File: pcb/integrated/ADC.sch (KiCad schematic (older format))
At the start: 18 parts, among them U6001 SG3225, U6002 AD9609

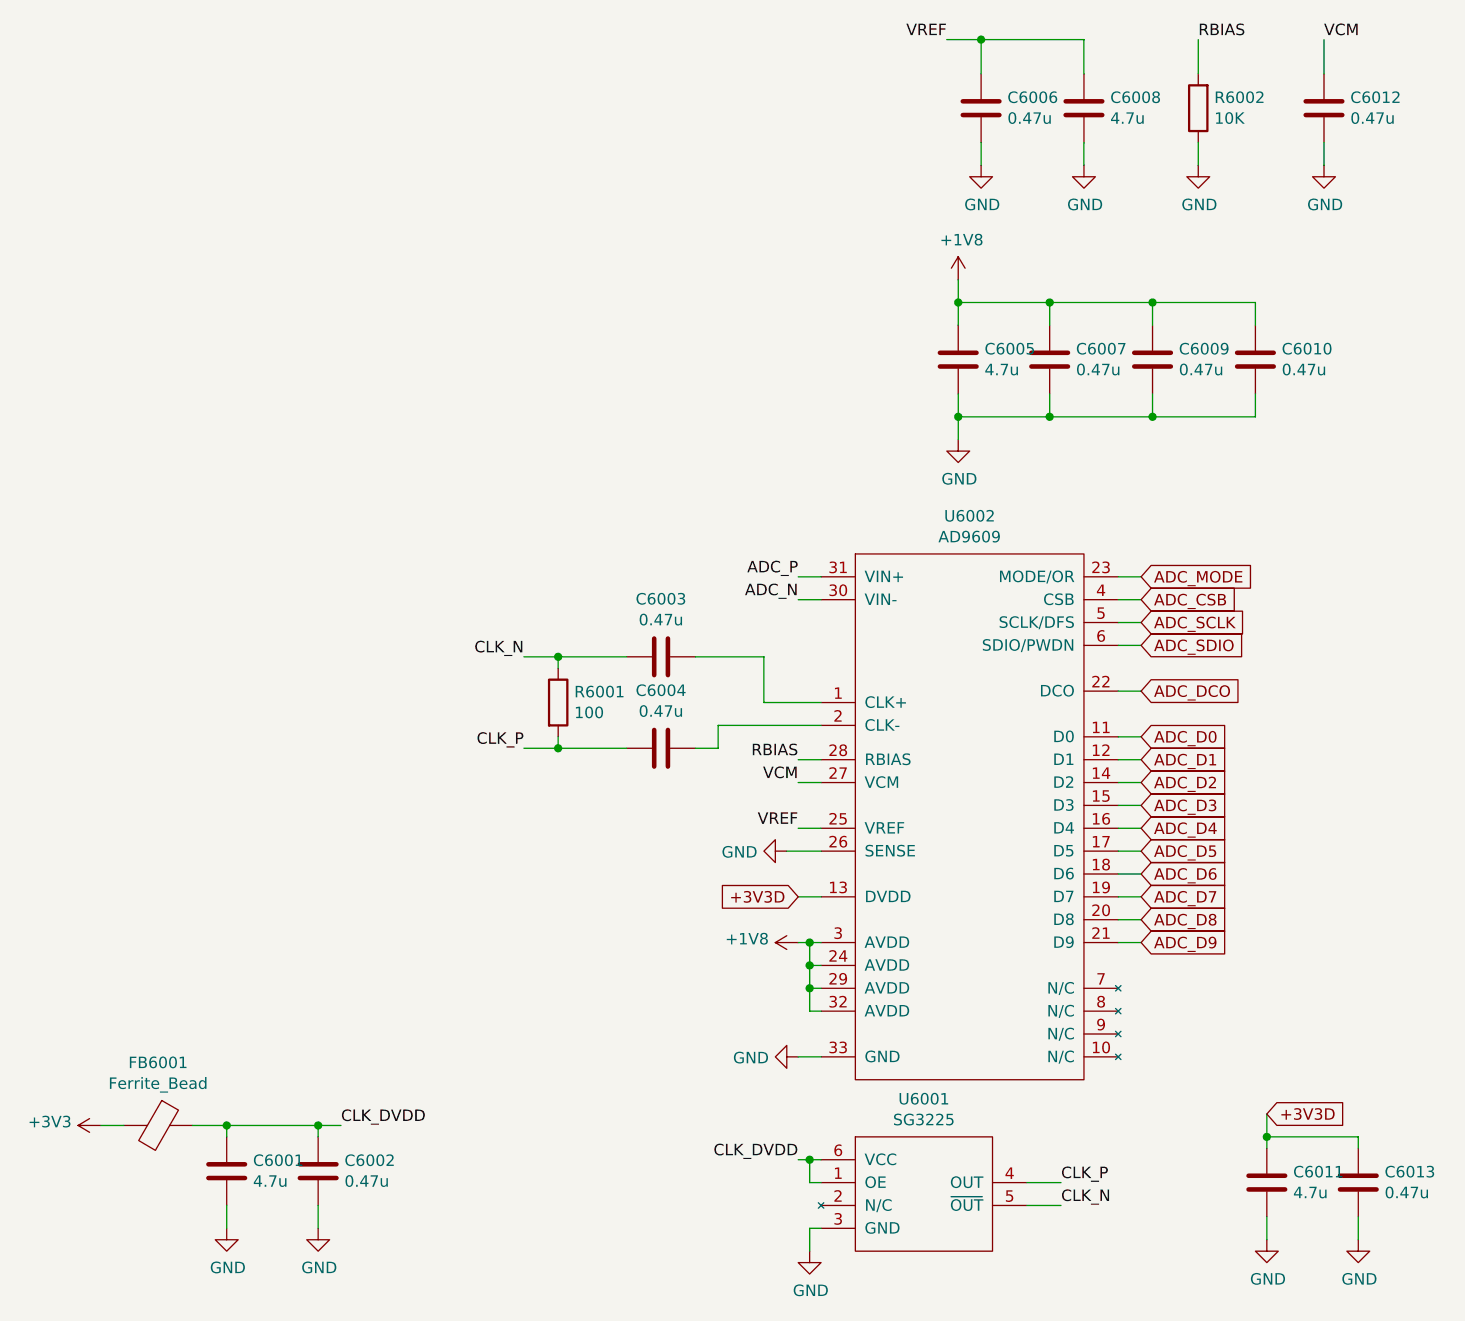
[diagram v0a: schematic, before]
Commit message: schematic fixes and component placement
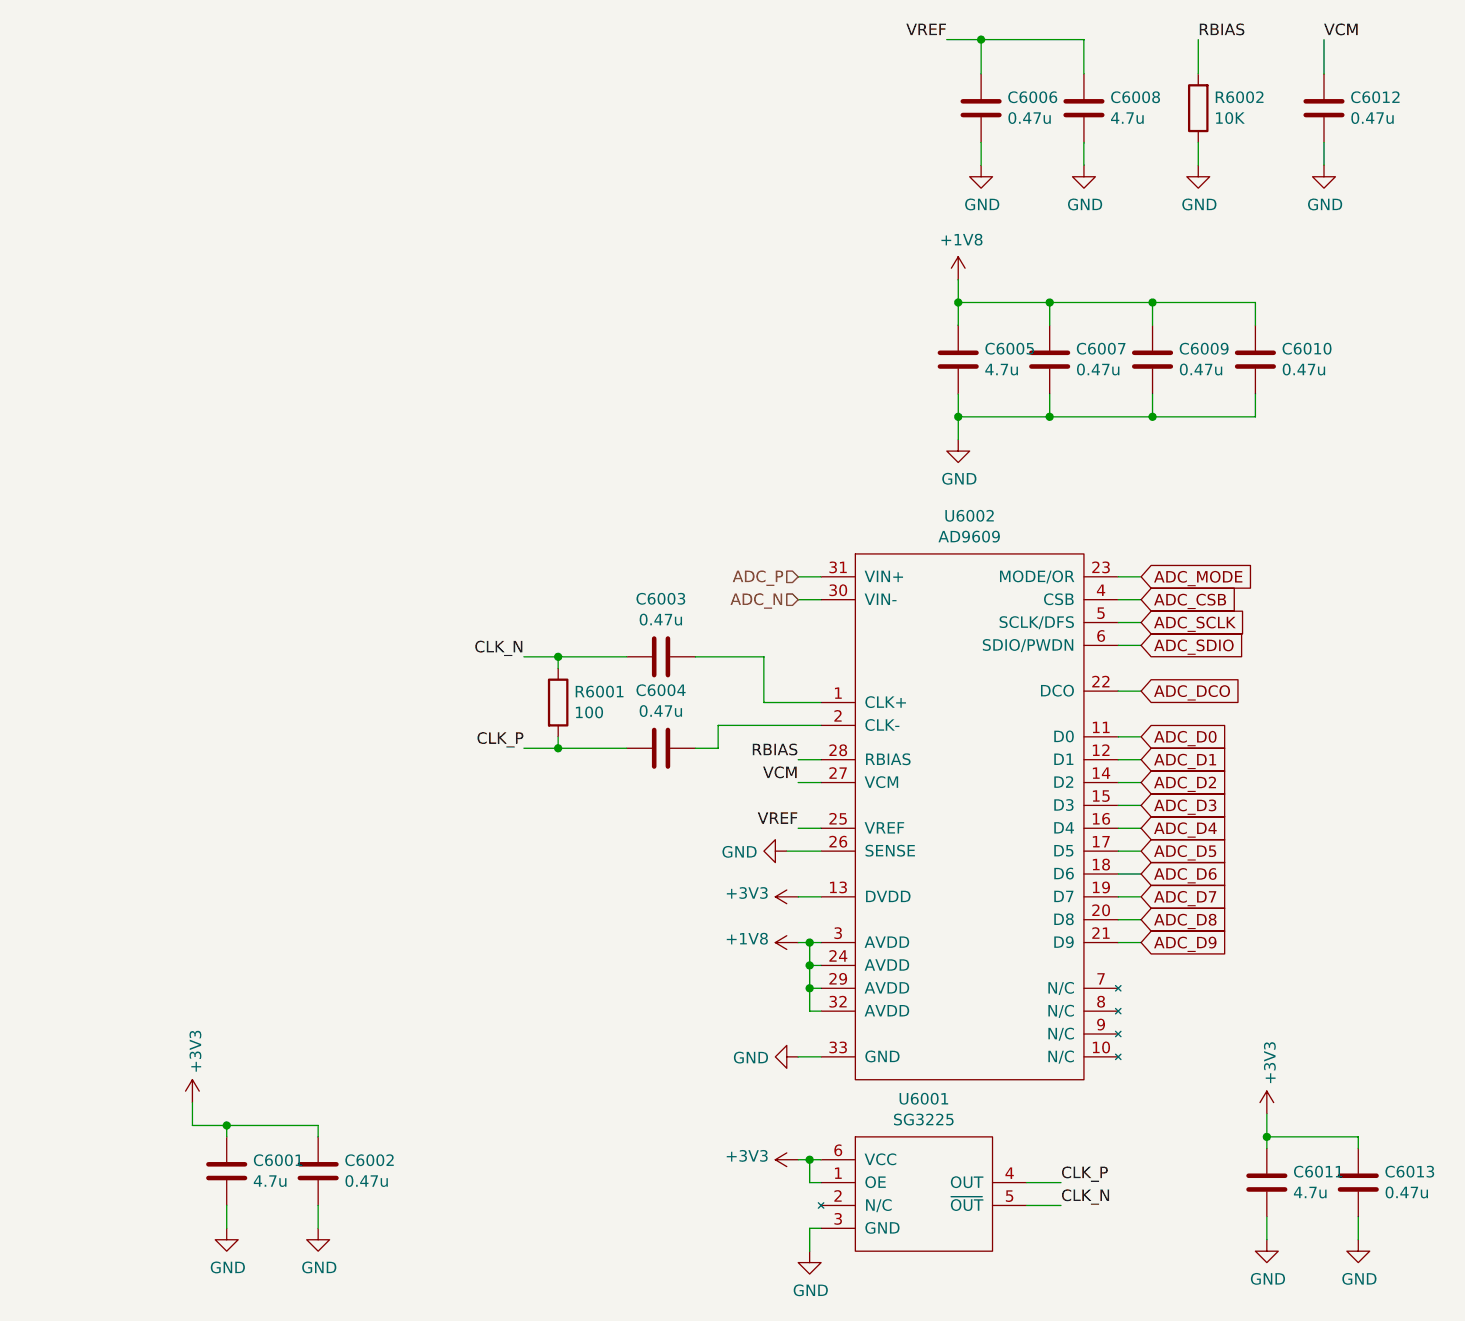
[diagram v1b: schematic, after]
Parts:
- removed FB6001: Ferrite_Bead, Inductor_SMD:L_0805_2012Metric, symbol Device:Ferrite_Bead
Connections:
- net +3V3D is gone; now on net +3V3: C6011.2, C6013.2, U6002.13 (DVDD)
- net CLK_DVDD is gone; now on net +3V3: C6001.2, C6002.2, U6001.1 (OE), U6001.6 (VCC)
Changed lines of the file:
@@
 Wire Wire Line
 	7850 3350 7750 3350
-Text Label 7750 3250 2    50   ~ 0
-ADC_P
-Text Label 7750 3350 2    50   ~ 0
-ADC_N
 Wire Wire Line
 	9150 3950 9250 3950
@@
 	1    0    0    -1
 $EndComp
-Text Label 7750 5800 2    50   ~ 0
-CLK_DVDD
 Text Label 8900 5900 0    50   ~ 0
 CLK_P
@@
 Text Label 6550 3600 2    50   ~ 0
 CLK_N
-Text GLabel 7750 4650 0    50   Input ~ 0
-+3V3D
 $Comp
 L Device:C C?
@@
 	9800 5700 9800 5600
 Connection ~ 9800 5700
-Text GLabel 9800 5600 2    50   Input ~ 0
-+3V3D
 $Comp
 L Device:C C?
@@
 $EndComp
 $Comp
-L Device:Ferrite_Bead FB?
-U 1 1 5D65D25A
-P 4950 5650
-AR Path="/5D33C768/5D33CBF6/5D65D25A" Ref="FB?"  Part="1"
-AR Path="/5D33C768/5D63A69A/5D65D25A" Ref="FB6001"  Part="1"
-F 0 "FB6001" V 4676 5650 50  0000 C CNN
-F 1 "Ferrite_Bead" V 4767 5650 50  0000 C CNN
-F 2 "Inductor_SMD:L_0805_2012Metric" V 4880 5650 50  0001 C CNN
-F 3 "~" H 4950 5650 50  0001 C CNN
-	1    4950 5650
-	0    1    1    0
-$EndComp
-$Comp
 L Device:C C?
 U 1 1 5D65D261
@@
 $EndComp
 Wire Wire Line
-	4800 5650 4700 5650
+	5100 5650 5100 5550
 $Comp
 L power:+3V3 #PWR?
 U 1 1 5D65D283
-P 4700 5650
+P 5100 5550
 AR Path="/5D33C768/5D33CBF6/5D65D283" Ref="#PWR?"  Part="1"
 AR Path="/5D33C768/5D63A69A/5D65D283" Ref="#PWR06001"  Part="1"
-F 0 "#PWR06001" H 4700 5500 50  0001 C CNN
-F 1 "+3V3" V 4715 5778 50  0000 L CNN
-F 2 "" H 4700 5650 50  0001 C CNN
-F 3 "" H 4700 5650 50  0001 C CNN
-	1    4700 5650
+F 0 "#PWR06001" H 5100 5400 50  0001 C CNN
+F 1 "+3V3" V 5115 5678 50  0000 L CNN
+F 2 "" H 5100 5550 50  0001 C CNN
+F 3 "" H 5100 5550 50  0001 C CNN
+	1    5100 5550
+	1    0    0    -1
+$EndComp
+Text HLabel 7750 3250 0    50   Input ~ 0
+ADC_P
+Text HLabel 7750 3350 0    50   Input ~ 0
+ADC_N
+$Comp
+L power:+3V3 #PWR?
+U 1 1 5D81D31E
+P 7750 4650
+AR Path="/5D33C768/5D33CBF6/5D81D31E" Ref="#PWR?"  Part="1"
+AR Path="/5D33C768/5D63A69A/5D81D31E" Ref="#PWR0173"  Part="1"
+F 0 "#PWR0173" H 7750 4500 50  0001 C CNN
+F 1 "+3V3" V 7765 4778 50  0000 L CNN
+F 2 "" H 7750 4650 50  0001 C CNN
+F 3 "" H 7750 4650 50  0001 C CNN
+	1    7750 4650
 	0    -1   -1   0
 $EndComp
-Wire Wire Line
-	5650 5650 5750 5650
-Connection ~ 5650 5650
-Text Label 5750 5650 0    50   ~ 0
-CLK_DVDD
+$Comp
+L power:+3V3 #PWR?
+U 1 1 5D81DA4C
+P 9800 5600
+AR Path="/5D33C768/5D33CBF6/5D81DA4C" Ref="#PWR?"  Part="1"
+AR Path="/5D33C768/5D63A69A/5D81DA4C" Ref="#PWR0174"  Part="1"
+F 0 "#PWR0174" H 9800 5450 50  0001 C CNN
+F 1 "+3V3" V 9815 5728 50  0000 L CNN
+F 2 "" H 9800 5600 50  0001 C CNN
+F 3 "" H 9800 5600 50  0001 C CNN
+	1    9800 5600
+	1    0    0    -1
+$EndComp
+$Comp
+L power:+3V3 #PWR?
+U 1 1 5D89B8AD
+P 7750 5800
+AR Path="/5D33C768/5D33CBF6/5D89B8AD" Ref="#PWR?"  Part="1"
+AR Path="/5D33C768/5D63A69A/5D89B8AD" Ref="#PWR0179"  Part="1"
+F 0 "#PWR0179" H 7750 5650 50  0001 C CNN
+F 1 "+3V3" V 7765 5928 50  0000 L CNN
+F 2 "" H 7750 5800 50  0001 C CNN
+F 3 "" H 7750 5800 50  0001 C CNN
+	1    7750 5800
+	0    -1   -1   0
+$EndComp
 $EndSCHEMATC
